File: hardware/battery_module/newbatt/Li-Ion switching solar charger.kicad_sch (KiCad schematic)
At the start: 16 parts, among them U3 BQ25570

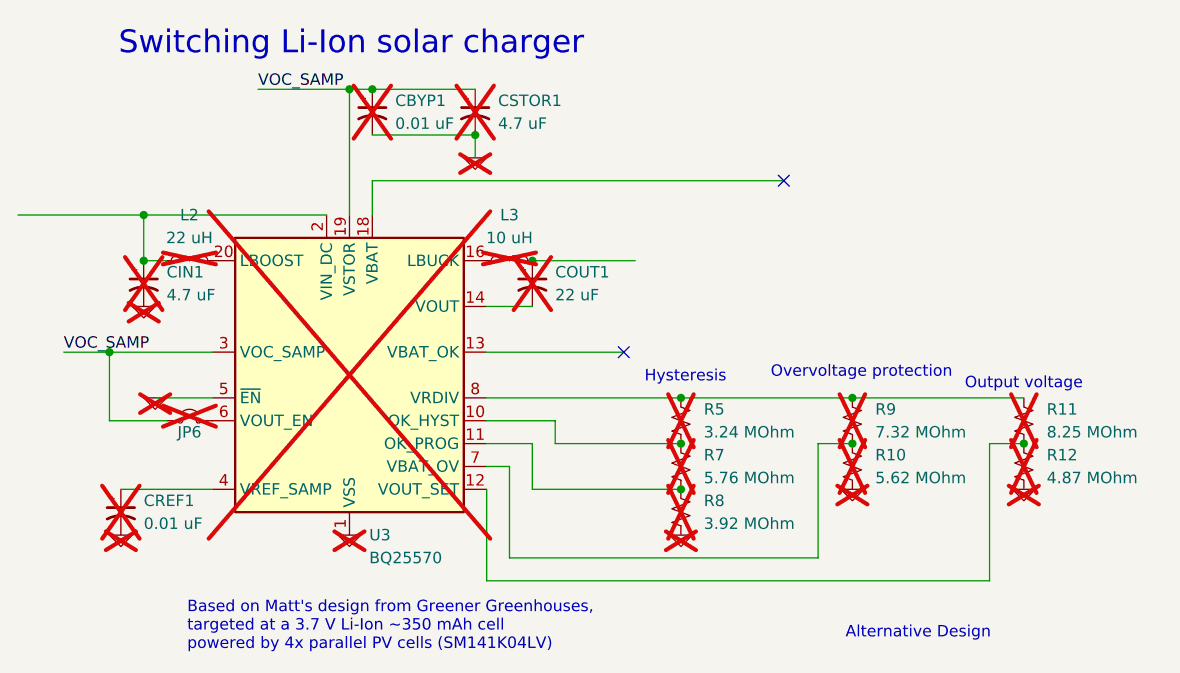
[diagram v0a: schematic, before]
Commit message: battery switch, fuse, and rerouted traces
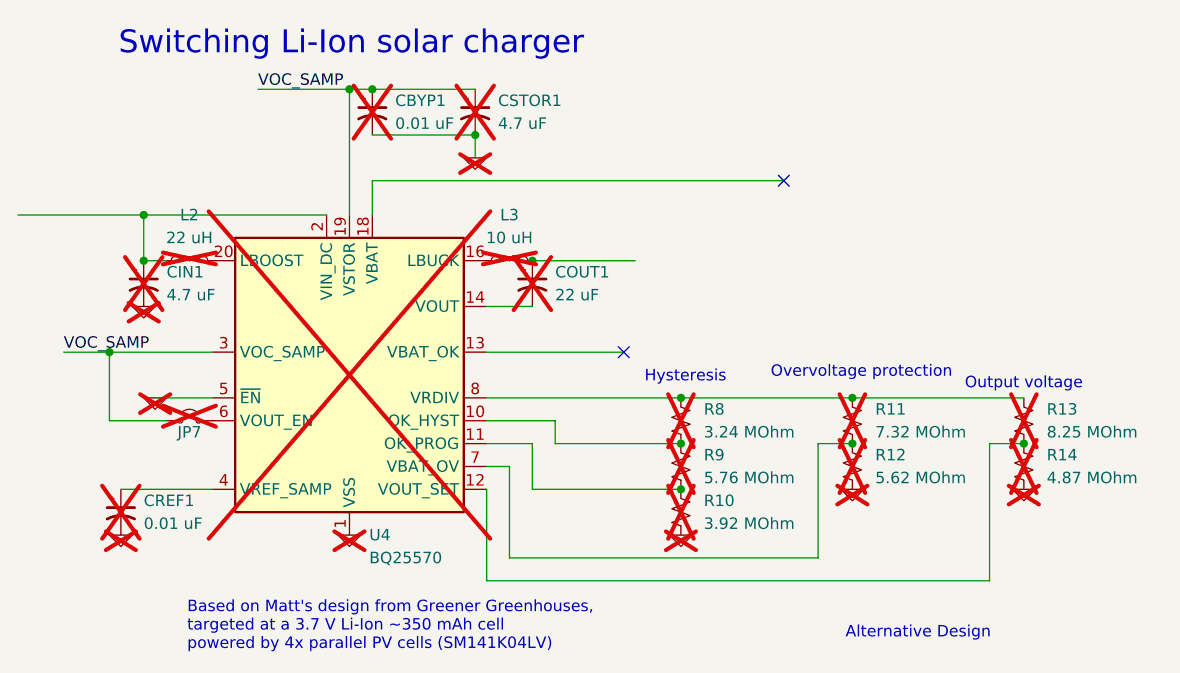
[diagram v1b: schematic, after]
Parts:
- renumbered JP6 to JP7, R8 to R10, R9 to R11, R10 to R12, R11 to R13, R12 to R14, R5 to R8, R7 to R9, U3 to U4
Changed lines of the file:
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@@
 		(dnp yes)
 		(fields_autoplaced yes)
-		(property "Reference" "U3"
+		(property "Reference" "U4"
 			(at 121.5741 105.41 0)
 			(effects
@@
 			(project "newbatt"
 				(path "/492e8d1d-dcc5-45c6-a3d2-2dfd8a06477e/6e1b4932-b662-4f76-aaf3-c122b2e64a12"
-					(reference "U3")
+					(reference "U4")
 					(unit 1)
 				)
@@
 		(dnp yes)
 		(fields_autoplaced yes)
-		(property "Reference" "R9"
+		(property "Reference" "R11"
 			(at 177.8 91.4399 0)
 			(effects
@@
 			(project "newbatt"
 				(path "/492e8d1d-dcc5-45c6-a3d2-2dfd8a06477e/6e1b4932-b662-4f76-aaf3-c122b2e64a12"
-					(reference "R9")
+					(reference "R11")
 					(unit 1)
 				)
@@
 		(dnp yes)
 		(fields_autoplaced yes)
-		(property "Reference" "R7"
+		(property "Reference" "R9"
 			(at 158.75 96.5199 0)
 			(effects
@@
 			(project "newbatt"
 				(path "/492e8d1d-dcc5-45c6-a3d2-2dfd8a06477e/6e1b4932-b662-4f76-aaf3-c122b2e64a12"
-					(reference "R7")
+					(reference "R9")
 					(unit 1)
 				)
@@
 		(dnp yes)
 		(fields_autoplaced yes)
-		(property "Reference" "#GND038"
+		(property "Reference" "#GND039"
 			(at 97.79 95.25 0)
 			(effects
@@
 			(project "newbatt"
 				(path "/492e8d1d-dcc5-45c6-a3d2-2dfd8a06477e/6e1b4932-b662-4f76-aaf3-c122b2e64a12"
-					(reference "#GND038")
+					(reference "#GND039")
 					(unit 1)
 				)
@@
 		(dnp yes)
 		(fields_autoplaced yes)
-		(property "Reference" "#GND042"
+		(property "Reference" "#GND043"
 			(at 175.26 105.41 0)
 			(effects
@@
 			(project "newbatt"
 				(path "/492e8d1d-dcc5-45c6-a3d2-2dfd8a06477e/6e1b4932-b662-4f76-aaf3-c122b2e64a12"
-					(reference "#GND042")
+					(reference "#GND043")
 					(unit 1)
 				)
@@
 		(dnp yes)
 		(fields_autoplaced yes)
-		(property "Reference" "#GND037"
+		(property "Reference" "#GND038"
 			(at 96.52 85.09 0)
 			(effects
@@
 			(project "newbatt"
 				(path "/492e8d1d-dcc5-45c6-a3d2-2dfd8a06477e/6e1b4932-b662-4f76-aaf3-c122b2e64a12"
-					(reference "#GND037")
+					(reference "#GND038")
 					(unit 1)
 				)
@@
 		(dnp yes)
 		(fields_autoplaced yes)
-		(property "Reference" "R11"
+		(property "Reference" "R13"
 			(at 196.85 91.4399 0)
 			(effects
@@
 			(project "newbatt"
 				(path "/492e8d1d-dcc5-45c6-a3d2-2dfd8a06477e/6e1b4932-b662-4f76-aaf3-c122b2e64a12"
-					(reference "R11")
+					(reference "R13")
 					(unit 1)
 				)
@@
 		(dnp yes)
 		(fields_autoplaced yes)
-		(property "Reference" "#GND041"
+		(property "Reference" "#GND042"
 			(at 156.21 110.49 0)
 			(effects
@@
 			(project "newbatt"
 				(path "/492e8d1d-dcc5-45c6-a3d2-2dfd8a06477e/6e1b4932-b662-4f76-aaf3-c122b2e64a12"
-					(reference "#GND041")
+					(reference "#GND042")
 					(unit 1)
 				)
@@
 		(dnp yes)
 		(fields_autoplaced yes)
-		(property "Reference" "#GND040"
+		(property "Reference" "#GND041"
 			(at 133.35 68.58 0)
 			(effects
@@
 			(project "newbatt"
 				(path "/492e8d1d-dcc5-45c6-a3d2-2dfd8a06477e/6e1b4932-b662-4f76-aaf3-c122b2e64a12"
-					(reference "#GND040")
+					(reference "#GND041")
 					(unit 1)
 				)
@@
 		(dnp yes)
 		(fields_autoplaced yes)
-		(property "Reference" "#GND039"
+		(property "Reference" "#GND040"
 			(at 119.38 110.49 0)
 			(effects
@@
 			(project "newbatt"
 				(path "/492e8d1d-dcc5-45c6-a3d2-2dfd8a06477e/6e1b4932-b662-4f76-aaf3-c122b2e64a12"
-					(reference "#GND039")
+					(reference "#GND040")
 					(unit 1)
 				)
@@
 		(dnp yes)
 		(fields_autoplaced yes)
-		(property "Reference" "R12"
+		(property "Reference" "R14"
 			(at 196.85 96.5199 0)
 			(effects
@@
 			(project "newbatt"
 				(path "/492e8d1d-dcc5-45c6-a3d2-2dfd8a06477e/6e1b4932-b662-4f76-aaf3-c122b2e64a12"
-					(reference "R12")
+					(reference "R14")
 					(unit 1)
 				)
@@
 		(dnp yes)
 		(fields_autoplaced yes)
-		(property "Reference" "#GND036"
+		(property "Reference" "#GND037"
 			(at 93.98 110.49 0)
 			(effects
@@
 			(project "newbatt"
 				(path "/492e8d1d-dcc5-45c6-a3d2-2dfd8a06477e/6e1b4932-b662-4f76-aaf3-c122b2e64a12"
-					(reference "#GND036")
+					(reference "#GND037")
 					(unit 1)
 				)
@@
 		(dnp yes)
 		(fields_autoplaced yes)
-		(property "Reference" "R8"
+		(property "Reference" "R10"
 			(at 158.75 101.5999 0)
 			(effects
@@
 			(project "newbatt"
 				(path "/492e8d1d-dcc5-45c6-a3d2-2dfd8a06477e/6e1b4932-b662-4f76-aaf3-c122b2e64a12"
-					(reference "R8")
+					(reference "R10")
 					(unit 1)
 				)
@@
 		(dnp yes)
 		(fields_autoplaced yes)
-		(property "Reference" "R5"
+		(property "Reference" "R8"
 			(at 158.75 91.4399 0)
 			(effects
@@
 			(project "newbatt"
 				(path "/492e8d1d-dcc5-45c6-a3d2-2dfd8a06477e/6e1b4932-b662-4f76-aaf3-c122b2e64a12"
-					(reference "R5")
+					(reference "R8")
 					(unit 1)
 				)
@@
 		(dnp yes)
 		(fields_autoplaced yes)
-		(property "Reference" "#GND043"
+		(property "Reference" "#GND044"
 			(at 194.31 105.41 0)
 			(effects
@@
 			(project "newbatt"
 				(path "/492e8d1d-dcc5-45c6-a3d2-2dfd8a06477e/6e1b4932-b662-4f76-aaf3-c122b2e64a12"
-					(reference "#GND043")
+					(reference "#GND044")
 					(unit 1)
 				)
@@
 		(on_board no)
 		(dnp yes)
-		(property "Reference" "JP6"
+		(property "Reference" "JP7"
 			(at 101.6 93.98 0)
 			(effects
@@
 			(project "newbatt"
 				(path "/492e8d1d-dcc5-45c6-a3d2-2dfd8a06477e/6e1b4932-b662-4f76-aaf3-c122b2e64a12"
-					(reference "JP6")
+					(reference "JP7")
 					(unit 1)
 				)
@@
 		(dnp yes)
 		(fields_autoplaced yes)
-		(property "Reference" "R10"
+		(property "Reference" "R12"
 			(at 177.8 96.5199 0)
 			(effects
@@
 			(project "newbatt"
 				(path "/492e8d1d-dcc5-45c6-a3d2-2dfd8a06477e/6e1b4932-b662-4f76-aaf3-c122b2e64a12"
-					(reference "R10")
-					(unit 1)
-				)
+					(reference "R12")
+					(unit 1)
+				)

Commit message: Updated BoM with LCSC, Digikey. Updated 18650 battery clip footprint with 67.2mm spacing for 65mm and 67mm cells
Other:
- title: (none) -> ENTS Node Battery Module
